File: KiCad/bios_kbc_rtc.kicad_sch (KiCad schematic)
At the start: 47 parts, among them J1 KEYBOARD, Q1 2N3906, Q2 2N3904, U1 8242KBD, U10 SIMM0, U11 SIMM1, U12 SIMM2, U13 SIMM3, U2 74HC05, U3 27C512, U4 HM6818A, U5 4069, X1 32768Hz

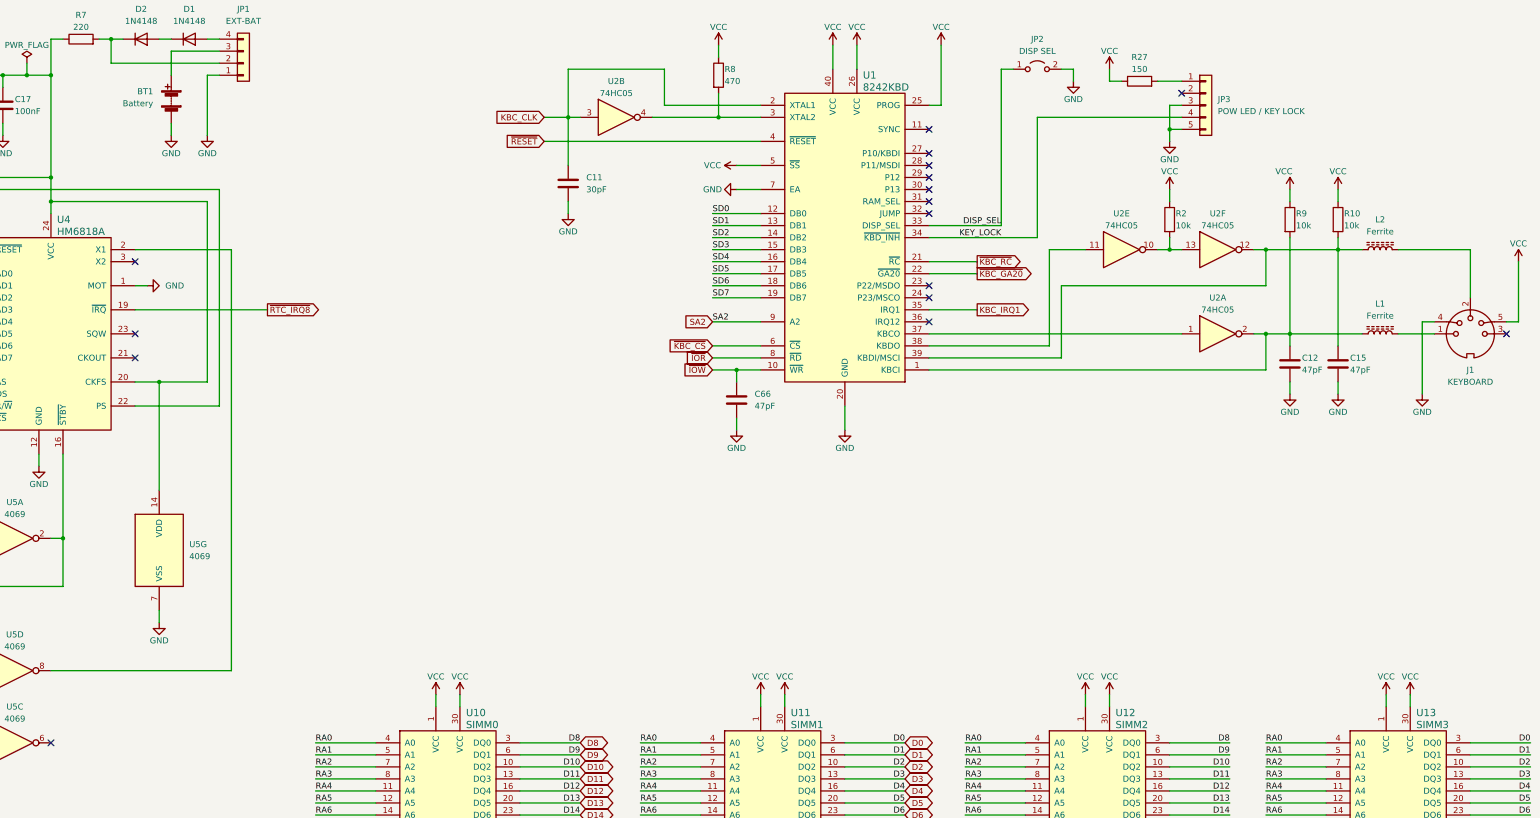
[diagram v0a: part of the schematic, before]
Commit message: Add R32, update footprints
Signed-off-by: Sergey Kiselev <skiselev@gmail.com>
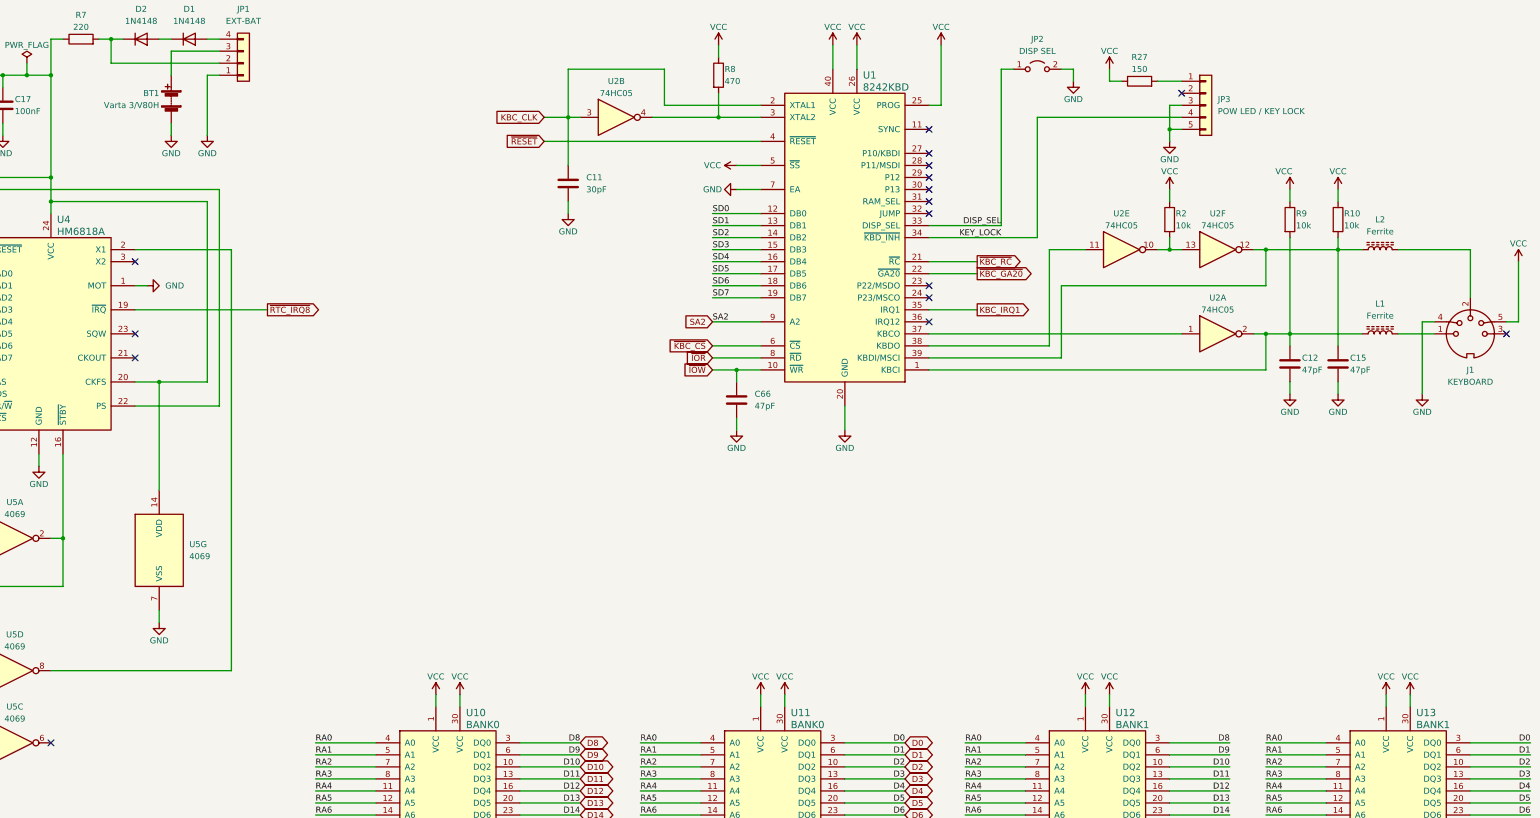
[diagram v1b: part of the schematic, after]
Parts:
- BT1: value Battery -> Varta 3/V80H
- U10: value SIMM0 -> BANK0
- U11: value SIMM1 -> BANK0
- U12: value SIMM2 -> BANK1
- U13: value SIMM3 -> BANK1
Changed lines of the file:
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@@
       (effects (font (size 1.524 1.524)) (justify left))
     )
-    (property "Value" "SIMM3" (id 1) (at 372.11 176.53 0)
+    (property "Value" "BANK1" (id 1) (at 372.11 176.53 0)
       (effects (font (size 1.524 1.524)) (justify left))
     )
@@
       (effects (font (size 1.524 1.524)) (justify left))
     )
-    (property "Value" "SIMM2" (id 1) (at 308.61 176.53 0)
+    (property "Value" "BANK1" (id 1) (at 308.61 176.53 0)
       (effects (font (size 1.524 1.524)) (justify left))
     )
@@
   )
   (symbol (lib_id "Device:Battery") (at 109.22 44.45 0) (mirror y) (unit 1)
-    (in_bom yes) (on_board yes) (fields_autoplaced)
-    (property "Reference" "BT1" (id 0) (at 105.41 42.7989 0)
-      (effects (font (size 1.27 1.27)) (justify left))
-    )
-    (property "Value" "Battery" (id 1) (at 105.41 45.3389 0)
+    (in_bom yes) (on_board yes)
+    (property "Reference" "BT1" (id 0) (at 106.68 43.18 0)
+      (effects (font (size 1.27 1.27)) (justify left))
+    )
+    (property "Value" "Varta 3/V80H" (id 1) (at 106.68 45.72 0)
       (effects (font (size 1.27 1.27)) (justify left))
     )
@@
       (effects (font (size 1.524 1.524)) (justify left))
     )
-    (property "Value" "SIMM0" (id 1) (at 171.45 176.53 0)
+    (property "Value" "BANK0" (id 1) (at 171.45 176.53 0)
       (effects (font (size 1.524 1.524)) (justify left))
     )
@@
       (effects (font (size 1.524 1.524)) (justify left))
     )
-    (property "Value" "SIMM1" (id 1) (at 240.03 176.53 0)
-      (effects (font (size 1.524 1.524)) (justify left))
-    )
+    (property "Value" "BANK0" (id 1) (at 240.03 176.53 0)
+      (effects (font (size 1.524 1.524)) (justify left))
+    )

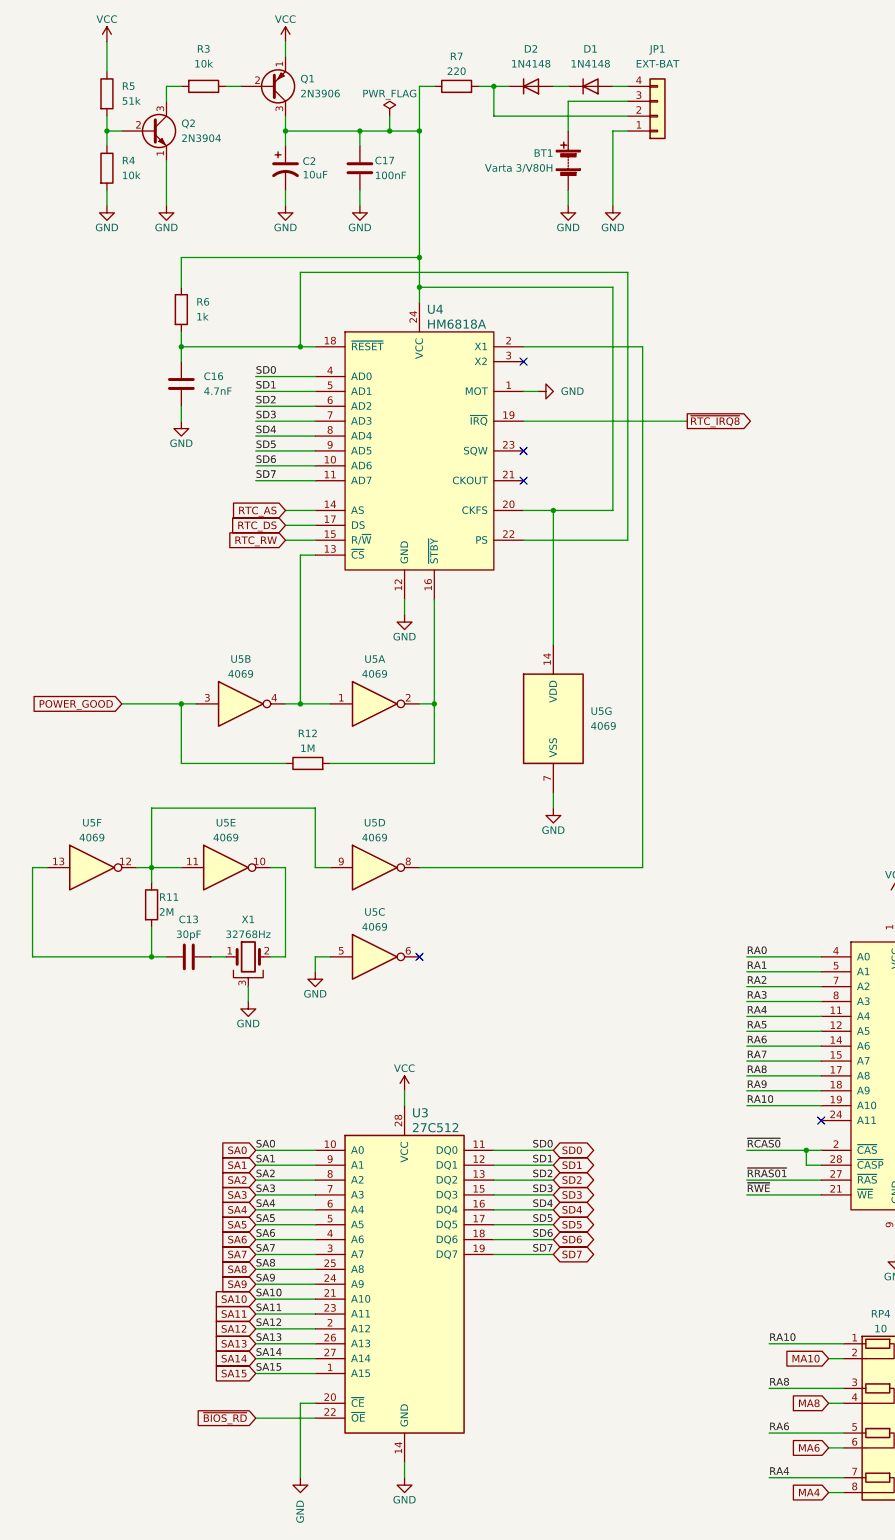
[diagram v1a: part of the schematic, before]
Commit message: Use DS12885 RTC
Signed-off-by: Sergey Kiselev <skiselev@gmail.com>
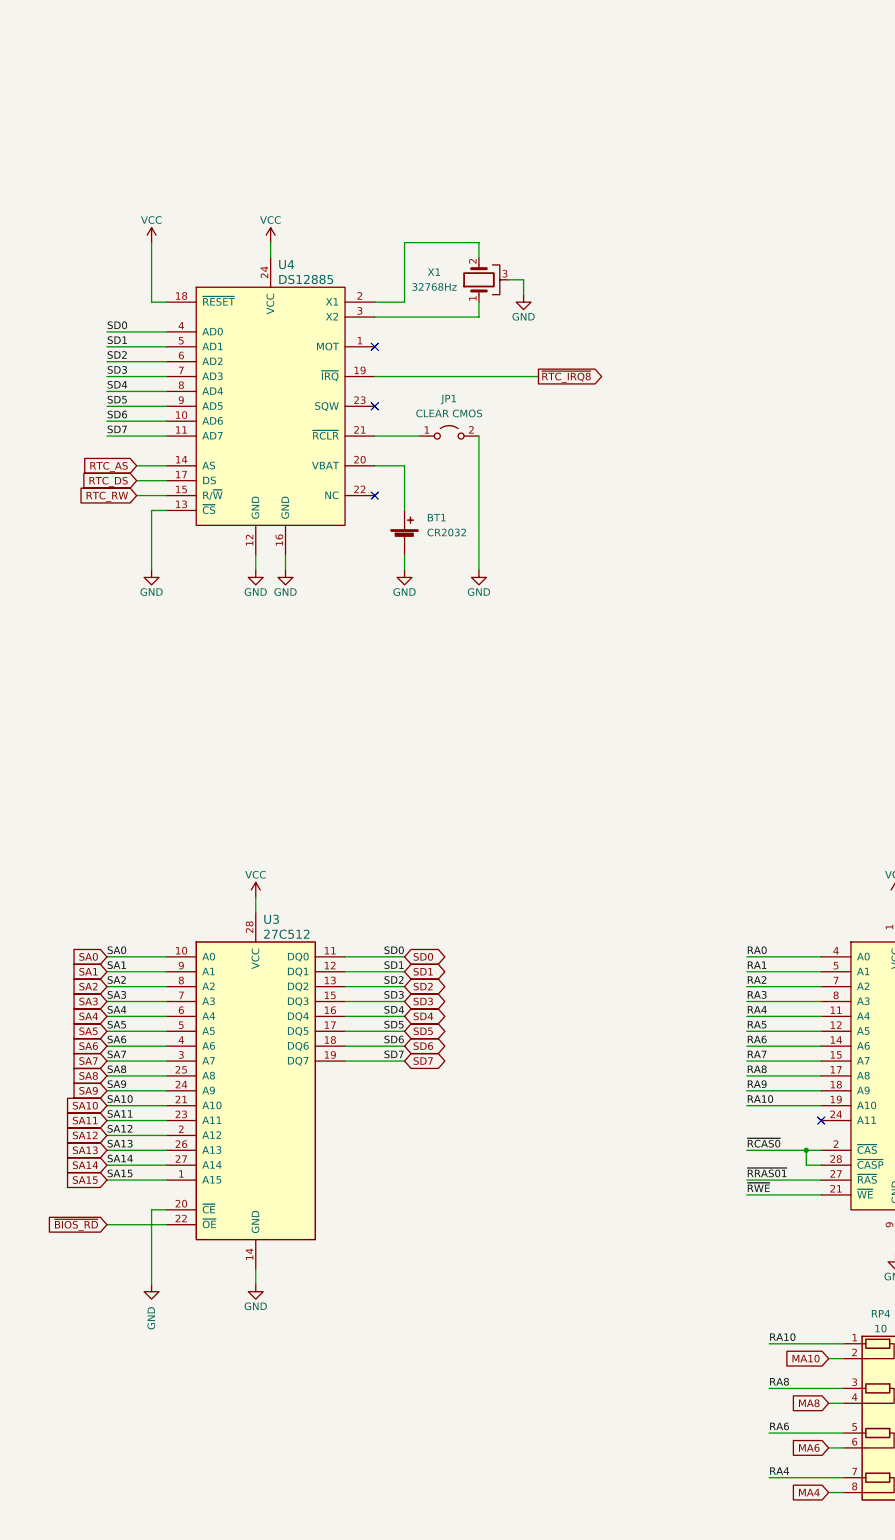
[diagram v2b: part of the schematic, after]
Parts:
- removed BT1: Varta 3/V80H, My_Components:Battery_Varta_3V80H, symbol Device:Battery
- removed C13: 30pF, My_Components:Cap_Cer_508, symbol Device:C
- removed C16: 4.7nF, My_Components:Cap_Cer_508, symbol Device:C
- removed C17: 100nF, My_Components:Cap_Cer_508, symbol Device:C
- removed C2: 10uF, My_Components:Cap_Elec_Radial_5mm_2.5mm, symbol Device:C_Polarized_US
- removed D1, D2: 1N4148, My_Components:Diode_1016, symbol Diode:1N4148
- removed JP1: EXT-BAT, My_Components:Conn_Pin_Header_4x1_2.54mm, symbol Connector_Generic:Conn_01x04
- removed Q1: 2N3906, My_Components:Transistor_TO92_EBC_254, symbol Transistor_BJT:2N3906
- removed Q2: 2N3904, My_Components:Transistor_TO92_EBC_254, symbol Transistor_BJT:2N3904
- removed R11: 2M, My_Components:Res_Axial_L6.3mm_D2.5mm_P10.16mm_Horizontal, symbol Device:R
- removed R12: 1M, My_Components:Res_Axial_L6.3mm_D2.5mm_P10.16mm_Horizontal, symbol Device:R
- removed R3, R4: 10k, My_Components:Res_Axial_L6.3mm_D2.5mm_P10.16mm_Horizontal, symbol Device:R
- removed R5: 51k, My_Components:Res_Axial_L6.3mm_D2.5mm_P10.16mm_Horizontal, symbol Device:R
- removed R6: 1k, My_Components:Res_Axial_L6.3mm_D2.5mm_P10.16mm_Horizontal, symbol Device:R
- removed R7: 220, My_Components:Res_Axial_L6.3mm_D2.5mm_P10.16mm_Horizontal, symbol Device:R
- removed U4: HM6818A, My_Components:IC_DIP24_600, symbol my_components:HM6818A
- removed U5: 4069, My_Components:IC_DIP14_300, symbol 4xxx:4069
- added BT1: CR2032, My_Components:Battery_Holder_CR2032_Universal, symbol Device:Battery_Cell
- added JP1: CLEAR CMOS, My_Components:Conn_Pin_Header_2x1_2.54mm, symbol Jumper:Jumper_2_Open
- added U4: DS12885, My_Components:IC_DIP24_600, symbol my_components:DS12885
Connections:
- net GND: now also BT1.2 (-), JP1.2 (B), U4.12 (GND), U4.13 (~{CS}), U4.16 (GND)
- net RTC_AS: now also U4.14 (AS)
- net RTC_DS: now also U4.17 (DS)
- net RTC_RW: now also U4.15 (R/~{W})
- net SD0: now also U4.4 (AD0)
- net SD1: now also U4.5 (AD1)
- net SD2: now also U4.6 (AD2)
- net SD3: now also U4.7 (AD3)
- net SD4: now also U4.8 (AD4)
- net SD5: now also U4.9 (AD5)
- net SD6: now also U4.10 (AD6)
- net SD7: now also U4.11 (AD7)
- net VCC: now also U4.18 (~{RESET}), U4.24 (VCC)
- net ~{RTC_IRQ8}: now also U4.19 (~{IRQ})
- net at X1.1: now also U4.3 (X2)
- net at X1.2: now also U4.2 (X1)
- new net: BT1.1 (+), U4.20 (VBAT)
- new net: JP1.1 (A), U4.21 (~{RCLR})
- no-connect marks 20 -> 19
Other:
- moved on the sheet: U3, X1

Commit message: Add support for 128 KiB Flash ROM ICs
Signed-off-by: Sergey Kiselev <skiselev@gmail.com>
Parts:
- removed U3: 27C512, My_Components:IC_DIP28_600, symbol my_components:27C512
- added U3: SST39SF010A, My_Components:IC_DIP32_600, symbol my_components:SST39SF010A
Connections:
- net GND: now also U3.16 (GND), U3.2 (A16), U3.22 (~{CE})
- net SA0: now also U3.12 (A0)
- net SA1: now also U3.11 (A1)
- net SA10: now also U3.23 (A10)
- net SA11: now also U3.25 (A11)
- net SA12: now also U3.4 (A12)
- net SA13: now also U3.28 (A13)
- net SA14: now also U3.29 (A14)
- net SA15: now also U3.3 (A15)
- net SA2: now also U3.10 (A2)
- net SA3: now also U3.9 (A3)
- net SA4: now also U3.8 (A4)
- net SA5: now also U3.7 (A5)
- net SA6: now also U3.6 (A6)
- net SA7: now also U3.5 (A7)
- net SA8: now also U3.27 (A8)
- net SA9: now also U3.26 (A9)
- net SD0: now also U3.13 (DQ0)
- net SD1: now also U3.14 (DQ1)
- net SD2: now also U3.15 (DQ2)
- net SD3: now also U3.17 (DQ3)
- net SD4: now also U3.18 (DQ4)
- net SD5: now also U3.19 (DQ5)
- net SD6: now also U3.20 (DQ6)
- net SD7: now also U3.21 (DQ7)
- net VCC: now also U3.30 (NC), U3.31 (~{WE}), U3.32 (VCC)
- net ~{BIOS_RD}: now also U3.24 (~{OE})
- no-connect marks 19 -> 20

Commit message: Version 1.3: Implement PS/2 mouse. Use PS/2 dualport pinout for the keyboard/mouse connector
Signed-off-by: Sergey Kiselev <skiselev@gmail.com>
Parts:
- removed J1: KEYBOARD, My_Components:Conn_DIN_5pin, symbol Connector:DIN-5_180degree
- removed R10, R2, R9: 10k, My_Components:Res_Axial_L6.3mm_D2.5mm_P10.16mm_Horizontal, symbol Device:R
- added C13, C16: 47pF, My_Components:Cap_Cer_508, symbol Device:C
- added J1: PS/2 Dual Port, My_Components:Conn_Mini_DIN_6pin, symbol Connector:Mini-DIN-6
- added L3, L4: Ferrite, My_Components:L_Ferrite_1016, symbol Device:L_Ferrite
- added RP8: 10k, My_Components:Conn_SIL5, symbol Device:R_Network04
- L1, L2: footprint My_Components:Res_1016 -> My_Components:L_Ferrite_1016
- R8: value 470 -> 10k; footprint My_Components:Res_Axial_L6.3mm_D2.5mm_P10.16mm_Horizontal -> My_Components:Res_762
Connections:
- net GND: now also R8.2, C13.2, C16.2, J1.3
- net KBC_CLK: now also U1.3 (XTAL2); no longer U1.2 (XTAL1), U2.3
- net VCC: now also J1.4, RP8.1 (common); no longer R8.1
- net KBDI: now reaches U2.10
- net KBDI: now also C15.1, L2.1, U1.27 (P10/KBDI), RP8.2 (R1); no longer U2.13
- net KB_CLOCK: now reaches L1.2
- net KB_CLOCK: now also J1.5
- net KB_DATA: now reaches L2.2
- net KB_DATA: now also J1.1
- net KBDO: now reaches U1.38 (KBDO), U2.11
- net KBCO: now reaches U1.37 (KBCO), U2.1
- net KBCI: now reaches C12.1, L1.1, U1.1 (KBCI), U2.2
- net KBCI: now also RP8.3 (R2)
- net MSCI: now reaches U1.39 (KBDI/MSCI), U2.12
- net MSCI: now also C16.1, L3.1, RP8.5 (R4); no longer C15.1, L2.1
- net MSD0: now reaches U1.23 (P22/MSDO)
- net MSD0: now also U2.3
- net MSC0: now reaches U1.24 (P23/MSCO)
- net MSC0: now also U2.13
- net MSDI: now reaches U1.28 (P11/MSDI)
- net MSDI: now also U2.4, C13.1, L4.1, RP8.4 (R3)
- net KBC_IRQ12: now reaches U1.36 (IRQ12)
- new net: R8.1, U1.2 (XTAL1)
- new net MS_CLOCK: J1.6, L3.2
- new net MS_DATA: J1.2, L4.2
- no-connect marks 20 -> 14
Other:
- moved on the sheet: C11, C12, C15, C66, JP2, JP3, L1, L2, R27, R8, U1, U2A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
